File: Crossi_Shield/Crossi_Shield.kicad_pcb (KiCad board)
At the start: 2 copper layers, 84 parts, among them IC1 TPS54540DDAR, IC2 TCAN1048AVDMTRQ1, IC3 TCAN1048AVDMTRQ1, IC4 TCAN1048AVDMTRQ1, J1 Raspberry_Pi_2_3, J2 10090926-P444VLF, SW1 SW_DIP_x01

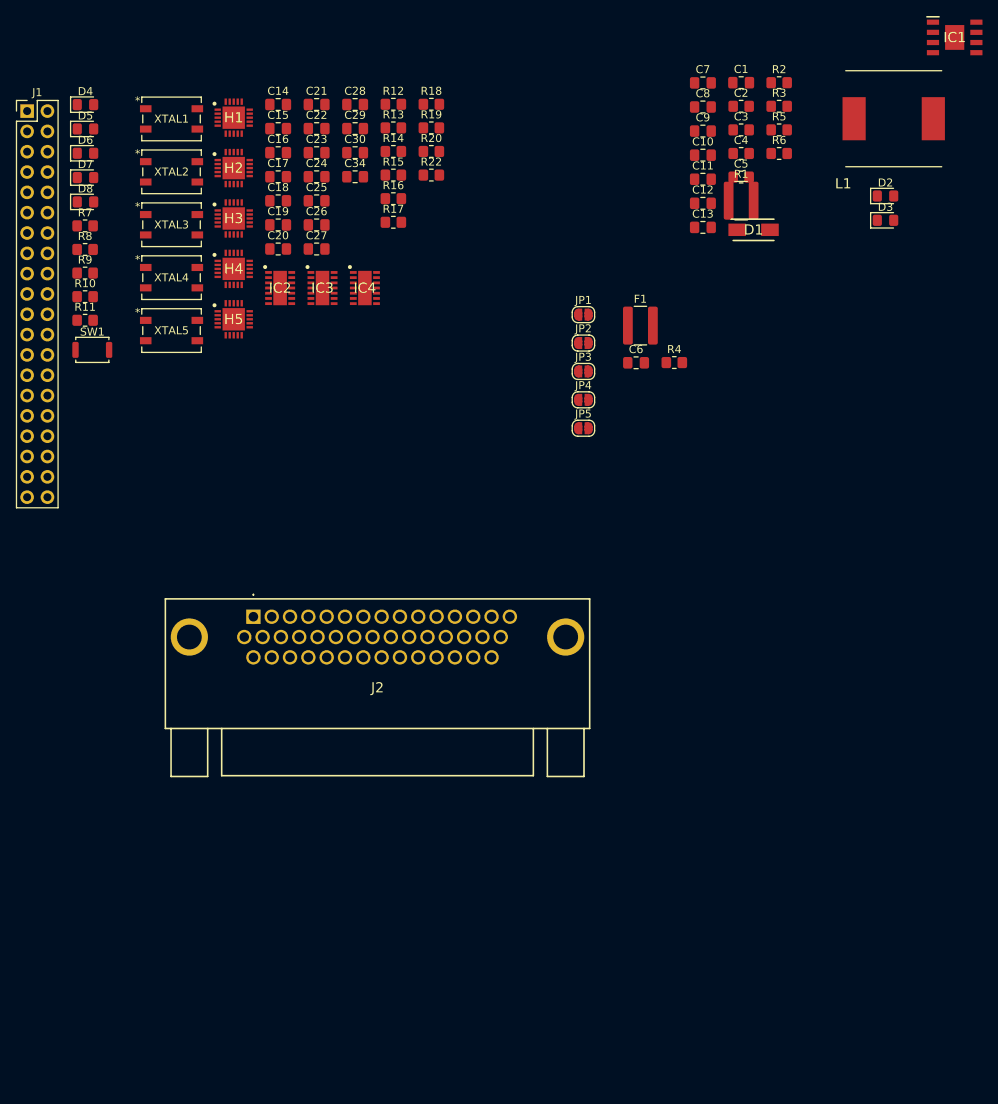
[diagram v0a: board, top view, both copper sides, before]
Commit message: add 5V and gnd
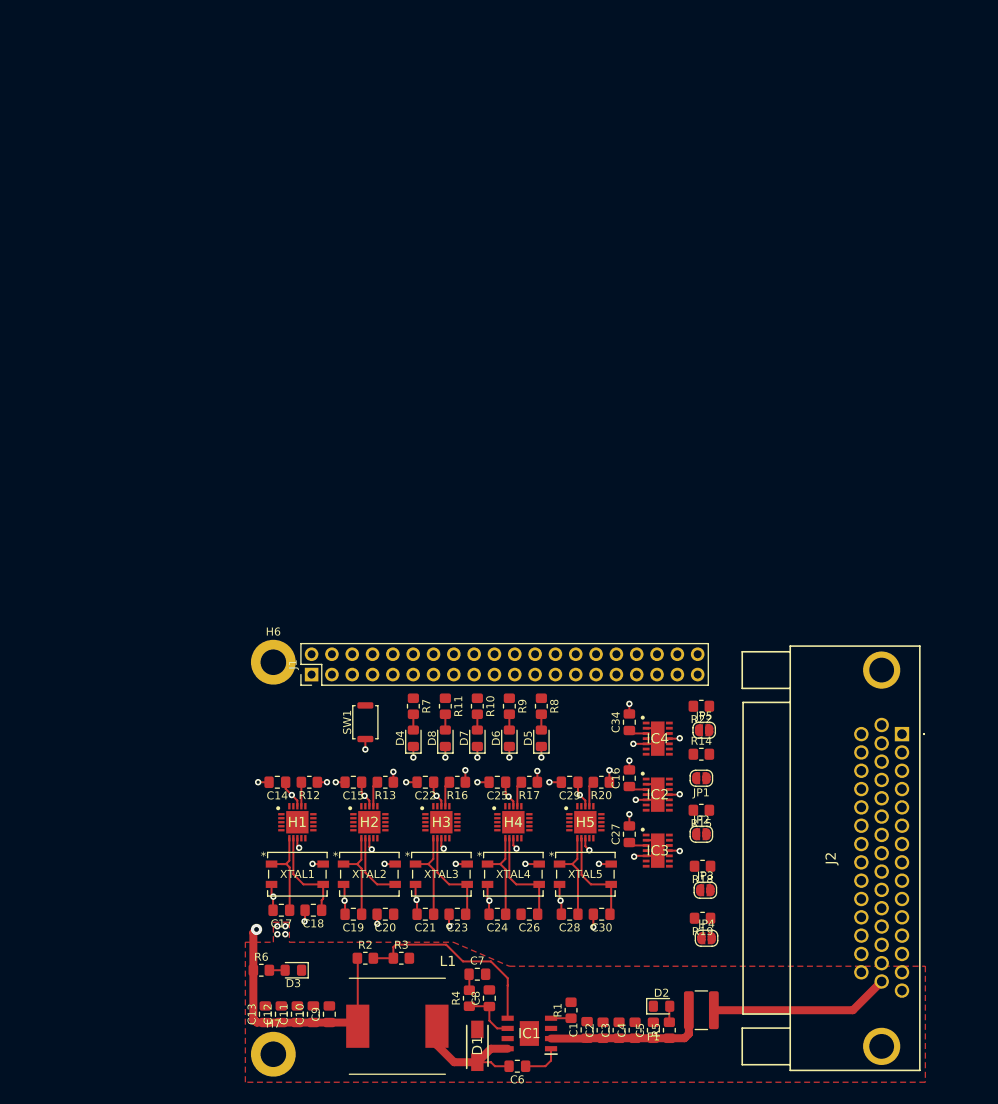
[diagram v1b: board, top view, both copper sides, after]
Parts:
- added H6: MountingHole, MountingHole:MountingHole_3.2mm_M3_DIN965_Pad, F.Cu at (83.5, 103.5)
- added H7: MountingHole, MountingHole:MountingHole_3.2mm_M3_DIN965_Pad, F.Cu at (83.5, 152.5)
- R1: footprint Resistor_SMD:R_1218_3246Metric_Pad1.22x4.75mm_HandSolder -> Resistor_SMD:R_0805_2012Metric_Pad1.20x1.40mm_HandSolder
- moved IC1 135.4 mm to (115.5, 149.9), turned to 180 degrees
- moved L1 129.3 mm to (99.0, 149.0), turned to 180 degrees
- moved R2 121.1 mm to (95.0, 140.5)
- moved R6 120.9 mm to (82.0, 142.0)
- moved C1 120.0 mm to (122.7, 149.5), turned to 90 degrees
- moved C9 119.9 mm to (90.5, 147.5), turned to 90 degrees
- moved D3 119.4 mm to (86.0, 142.0), turned to 180 degrees
- moved C10 117.9 mm to (88.5, 147.5), turned to 90 degrees
- moved C2 116.8 mm to (124.7, 149.5), turned to 90 degrees
- moved R3 116.5 mm to (99.5, 140.5)
- moved C11 116.0 mm to (86.5, 147.5), turned to 90 degrees
- moved C7 114.9 mm to (109.0, 142.5)
- moved C8 114.6 mm to (110.5, 145.5), turned to 90 degrees
- moved C12 114.2 mm to (84.5, 147.5), turned to 90 degrees
- moved C3 113.6 mm to (126.7, 149.5), turned to 90 degrees
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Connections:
- JP2 pad 1: unconnected-(JP2-A-Pad1) -> Net-(H1-RXCAN)
- JP3 pad 1: unconnected-(JP3-A-Pad1) -> Net-(H3-RXCAN)
- JP5 pad 1: unconnected-(JP5-A-Pad1) -> Net-(H5-RXCAN)
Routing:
- net GND: track 0.00 -> 74.6 mm, vias 0 -> 40
- net +5V: track 0.00 -> 68.2 mm, vias 0 -> 14
- net Net-(IC1-FB): track 0.00 -> 25.1 mm
- net /Versorgung/VIN: track 0.00 -> 22.5 mm
- net /Versorgung/VIN_SAVE: track 0.00 -> 20.4 mm
- net Net-(IC1-SW): track 0.00 -> 16.9 mm
- net Net-(H4-OSC1): track 0.00 -> 12.8 mm
- net Net-(H5-OSC1): track 0.00 -> 12.6 mm
- net Net-(H3-OSC1): track 0.00 -> 12.4 mm
- net Net-(H1-OSC1): track 0.00 -> 12.1 mm
- net Net-(H1-OSC2): track 0.00 -> 11.8 mm
- net Net-(H2-OSC2): track 0.00 -> 11.7 mm
- net Net-(H5-OSC2): track 0.00 -> 11.6 mm
- net Net-(H4-OSC2): track 0.00 -> 11.6 mm
- net Net-(H3-OSC2): track 0.00 -> 11.6 mm
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- added copper zone on In1.Cu, net +5V
- added copper zone on F.Cu, net GND
- added copper zone on In2.Cu, net GND
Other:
- copper layers 2 -> 4
